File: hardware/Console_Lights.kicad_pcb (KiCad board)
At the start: 2 copper layers, 0 parts

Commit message: creat lib, add footprints, schematic updates
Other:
- board outline added: 60 x 20 mm
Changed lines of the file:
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@@
     (area 0 0 0 0)
     (thickness 1.6)
-    (drawings 0)
+    (drawings 4)
     (tracks 0)
     (zones 0)
@@
     (uvia_drill 0.1)
   )
+  (gr_line (start 110 110) (end 110 90) (layer Edge.Cuts) (width 0.15))
+  (gr_line (start 170 110) (end 110 110) (layer Edge.Cuts) (width 0.15))
+  (gr_line (start 170 90) (end 170 110) (layer Edge.Cuts) (width 0.15))
+  (gr_line (start 110 90) (end 170 90) (layer Edge.Cuts) (width 0.15))
 )

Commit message: add footprints, BOM, schematic updates
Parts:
- added REF**: POST, ConsoleLights:POST, F.Cu at (158.1, 113.0)
- added REF**: POST, ConsoleLights:POST, F.Cu at (120.0, 113.0)
- added REF**: POST, ConsoleLights:POST, F.Cu at (158.1, 94.0)
- added REF**: POST, ConsoleLights:POST, F.Cu at (120.0, 94.0)
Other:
- board size 60 x 20 mm -> 60 x 30 mm
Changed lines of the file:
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@@
     (links 0)
     (no_connects 0)
-    (area 0 0 0 0)
+    (area 109.924999 89.924999 170.075001 110.075001)
     (thickness 1.6)
     (drawings 4)
     (tracks 0)
     (zones 0)
-    (modules 0)
+    (modules 4)
     (nets 1)
   )
@@
     (uvia_drill 0.1)
   )
-  (gr_line (start 110 110) (end 110 90) (layer Edge.Cuts) (width 0.15))
-  (gr_line (start 170 110) (end 110 110) (layer Edge.Cuts) (width 0.15))
-  (gr_line (start 170 90) (end 170 110) (layer Edge.Cuts) (width 0.15))
+  (module ConsoleLights:POST (layer F.Cu)
+    (at 158.1 113.05)
+    (fp_text reference REF** (at 0 3) (layer F.SilkS)
+      (effects (font (size 1 1) (thickness 0.15)))
+    )
+    (fp_text value POST (at 0 -3) (layer F.Fab)
+      (effects (font (size 1 1) (thickness 0.15)))
+    )
+    (pad 0 thru_hole circle (at 0 0) (size 4.2 4.2) (drill 2.2) (layers *.Cu *.Mask))
+  )
+  (module ConsoleLights:POST (layer F.Cu)
+    (at 120 113.05)
+    (fp_text reference REF** (at 0 3) (layer F.SilkS)
+      (effects (font (size 1 1) (thickness 0.15)))
+    )
+    (fp_text value POST (at 0 -3) (layer F.Fab)
+      (effects (font (size 1 1) (thickness 0.15)))
+    )
+    (pad 0 thru_hole circle (at 0 0) (size 4.2 4.2) (drill 2.2) (layers *.Cu *.Mask))
+  )
+  (module ConsoleLights:POST (layer F.Cu)
+    (at 158.1 94)
+    (fp_text reference REF** (at 0 3) (layer F.SilkS)
+      (effects (font (size 1 1) (thickness 0.15)))
+    )
+    (fp_text value POST (at 0 -3) (layer F.Fab)
+      (effects (font (size 1 1) (thickness 0.15)))
+    )
+    (pad 0 thru_hole circle (at 0 0) (size 4.2 4.2) (drill 2.2) (layers *.Cu *.Mask))
+  )
+  (module ConsoleLights:POST (layer F.Cu)
+    (at 120 94)
+    (fp_text reference REF** (at 0 3) (layer F.SilkS)
+      (effects (font (size 1 1) (thickness 0.15)))
+    )
+    (fp_text value POST (at 0 -3) (layer F.Fab)
+      (effects (font (size 1 1) (thickness 0.15)))
+    )
+    (pad 0 thru_hole circle (at 0 0) (size 4.2 4.2) (drill 2.2) (layers *.Cu *.Mask))
+  )
+  (gr_line (start 110 120) (end 110 90) (layer Edge.Cuts) (width 0.15))
+  (gr_line (start 170 120) (end 110 120) (layer Edge.Cuts) (width 0.15))
+  (gr_line (start 170 90) (end 170 120) (layer Edge.Cuts) (width 0.15))
   (gr_line (start 110 90) (end 170 90) (layer Edge.Cuts) (width 0.15))
 )

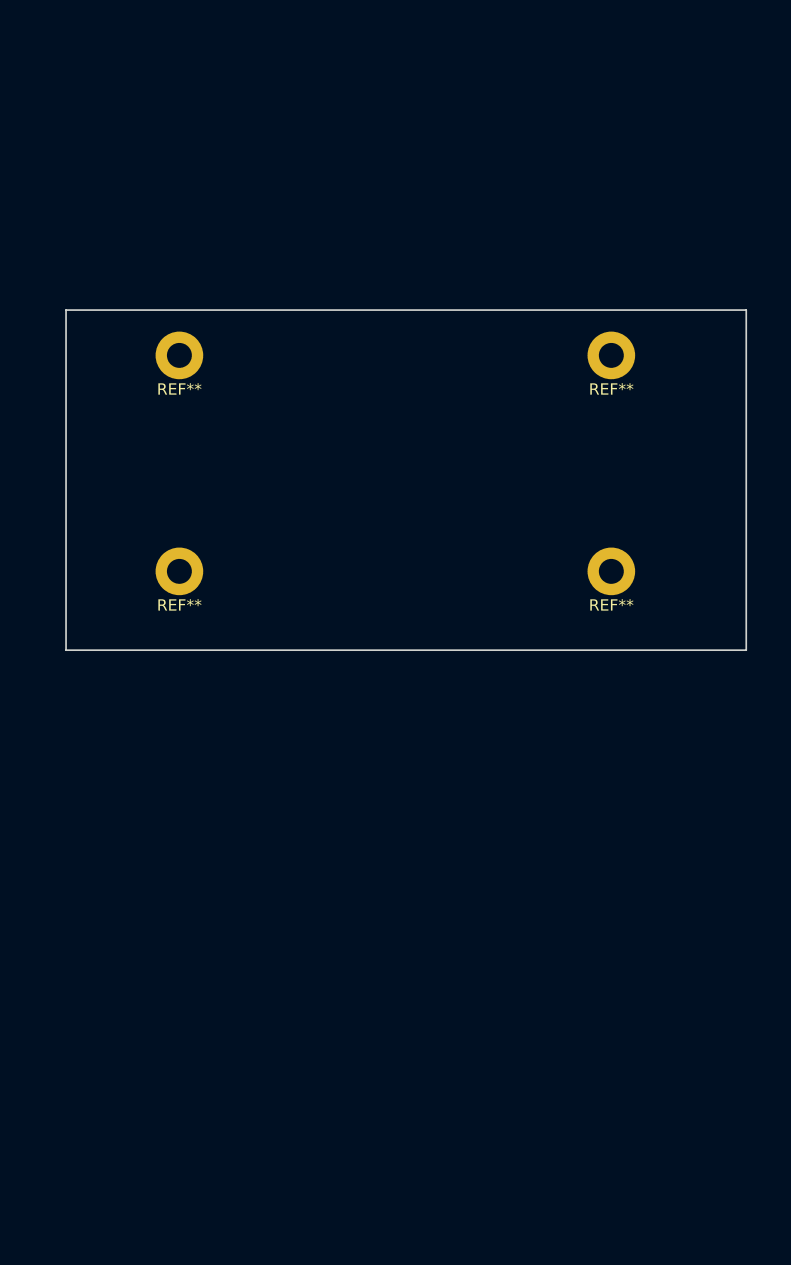
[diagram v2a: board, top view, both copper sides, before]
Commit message: BOM, footprint updates
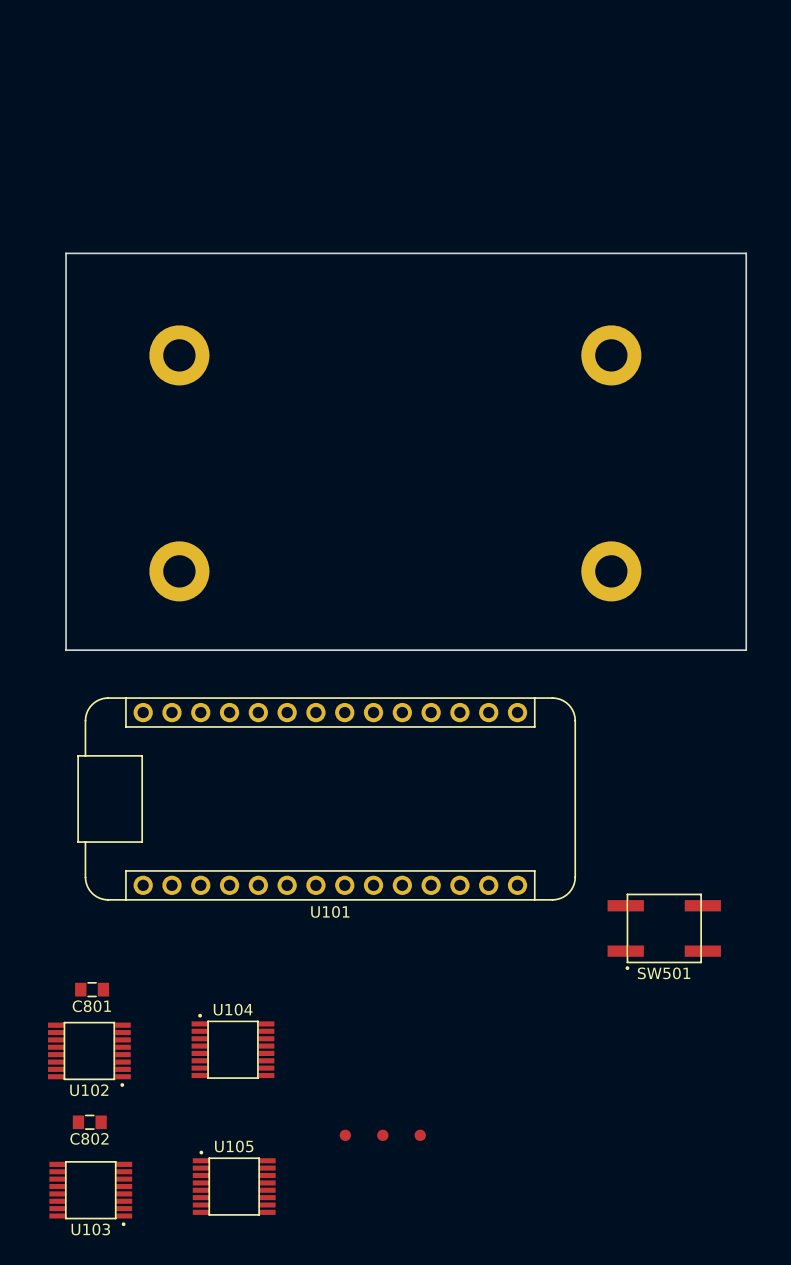
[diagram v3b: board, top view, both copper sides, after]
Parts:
- added C801: 1uF, ConsoleLights:C_0603, F.Cu at (112.3, 149.9)
- added C802: 1uF, ConsoleLights:C_0603, F.Cu at (112.1, 161.6)
- added SW501: SWITCH, ConsoleLights:Panasonic_Tac_Switch_EVQ-Q2K03W, F.Cu at (162.8, 144.5)
- added U101: Metro_Mini, ConsoleLights:Metro_Mini, F.Cu at (133.3, 133.1)
- added U102: 74HC595_SHIFT_REGISTER, ConsoleLights:16-TSSOP, F.Cu at (112.1, 155.4)
- added U103: 74HC595_SHIFT_REGISTER, ConsoleLights:16-TSSOP, F.Cu at (112.2, 167.6)
- added U104: ULN2003A_DARLINGTON_ARRAY, ConsoleLights:16-TSSOP, F.Cu at (124.7, 155.2)
- added U105: ULN2003A_DARLINGTON_ARRAY, ConsoleLights:16-TSSOP, F.Cu at (124.8, 167.3)
- added fid1: FID, ConsoleLights:Fiducial, F.Cu at (134.6, 162.8)
- added fid2: FID, ConsoleLights:Fiducial, F.Cu at (137.9, 162.8)
- added fid3: FID, ConsoleLights:Fiducial, F.Cu at (141.2, 162.8)
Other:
- board size 60 x 30 mm -> 60 x 35 mm

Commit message: add regulator, BOM, schematic, layout updates
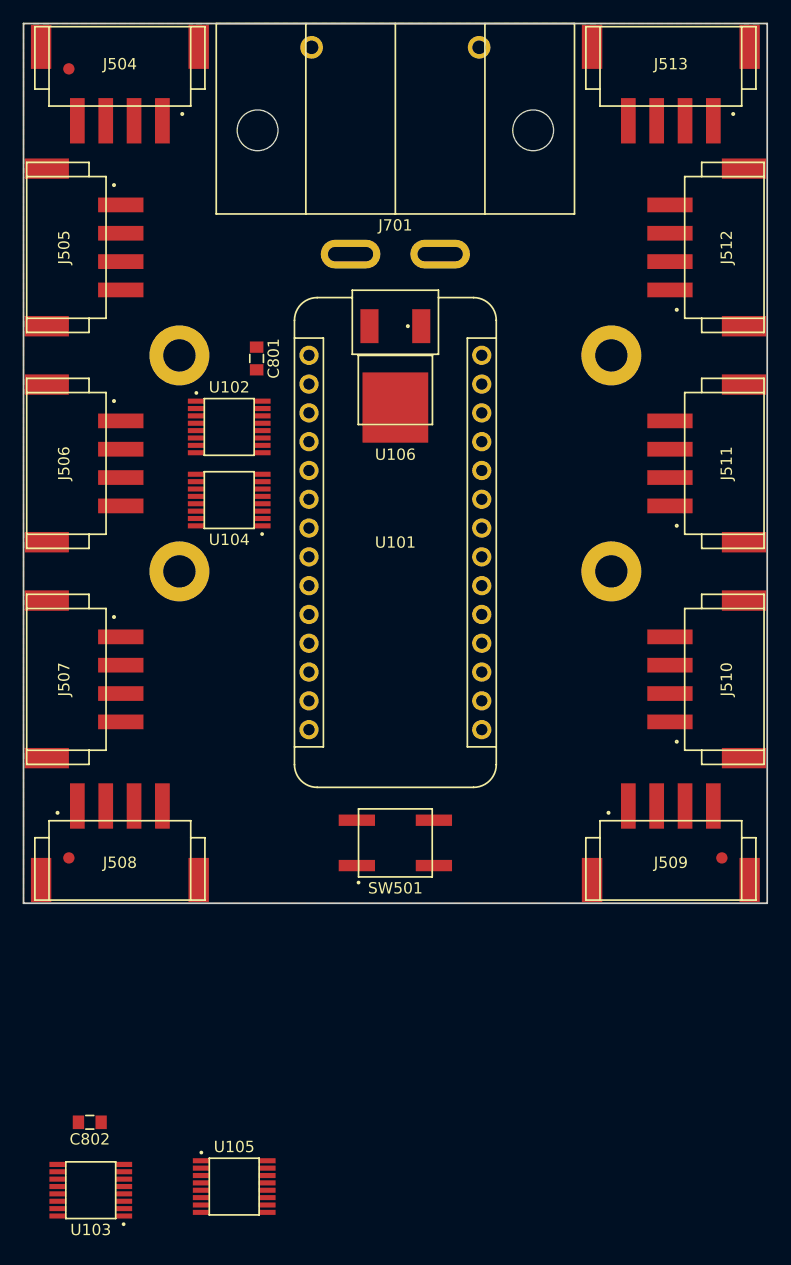
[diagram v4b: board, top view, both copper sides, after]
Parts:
- added J504: JST_Conn, ConsoleLights:S4B-XH-SM4-TB, F.Cu at (114.8, 64.7)
- added J505: JST_Conn, ConsoleLights:S4B-XH-SM4-TB, F.Cu at (106.2, 84.5)
- added J506: JST_Conn, ConsoleLights:S4B-XH-SM4-TB, F.Cu at (106.2, 103.5)
- added J507: JST_Conn, ConsoleLights:S4B-XH-SM4-TB, F.Cu at (106.2, 122.6)
- added J508: JST_Conn, ConsoleLights:S4B-XH-SM4-TB, F.Cu at (114.8, 142.3)
- added J509: JST_Conn, ConsoleLights:S4B-XH-SM4-TB, F.Cu at (163.3, 142.3)
- added J510: JST_Conn, ConsoleLights:S4B-XH-SM4-TB, F.Cu at (171.9, 122.6)
- added J511: JST_Conn, ConsoleLights:S4B-XH-SM4-TB, F.Cu at (171.9, 103.5)
- added J512: JST_Conn, ConsoleLights:S4B-XH-SM4-TB, F.Cu at (171.9, 84.5)
- added J513: JST_Conn, ConsoleLights:S4B-XH-SM4-TB, F.Cu at (163.3, 64.7)
- added J701: Conn_01x02, ConsoleLights:ASMPR45-1X2-RK_Wings, F.Cu at (139.1, 81.5)
- added U106: NCP1117-5_DPAK, ConsoleLights:DPAK_TO-252, F.Cu at (139.1, 95.5)
- moved fid1 97.2 mm to (110.2, 68.7)
- moved C801 57.5 mm to (126.8, 94.3), turned to 90 degrees
- moved U102 56.4 mm to (124.4, 100.3), turned to 0 degrees
- moved U104 48.5 mm to (124.4, 106.8), turned to 180 degrees
- moved fid2 37.0 mm to (110.2, 138.3)
- moved fid3 36.1 mm to (167.8, 138.3)
- moved SW501 24.9 mm to (139.1, 137.0)
- moved U101 23.3 mm to (139.1, 110.5), turned to 270 degrees
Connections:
- net Net-(U101-Pad10) renamed /SWITCH_8
- net Net-(U101-Pad12) renamed /SWITCH_9
- net Net-(U101-Pad7) renamed /SWITCH_5
- net Net-(U101-Pad8) renamed /SWITCH_6
- net Net-(U101-Pad9) renamed /SWITCH_7
- net Net-(U104-Pad10) renamed /LED_6
- net Net-(U104-Pad11) renamed /LED_5
- net Net-(U105-Pad14) renamed /LED_9
- net Net-(U105-Pad15) renamed /LED_8
- net Net-(U105-Pad16) renamed /LED_7
- SW501 pad 1: Net-(SW501-Pad1) -> GND
- SW501 pad 2: Net-(SW501-Pad2) -> /MODE
- U101 pad 19: Net-(U101-Pad19) -> /MODE
- U101 pad 2: Net-(U101-Pad2) -> /SWITCH_0
- U101 pad 26: Net-(U101-Pad26) -> +5V
- U101 pad 3: Net-(U101-Pad3) -> /SWITCH_1
- U101 pad 4: Net-(U101-Pad4) -> /SWITCH_2
- U101 pad 5: Net-(U101-Pad5) -> /SWITCH_3
- U101 pad 6: Net-(U101-Pad6) -> /SWITCH_4
- U104 pad 12: Net-(U104-Pad12) -> /LED_4
- U104 pad 13: Net-(U104-Pad13) -> /LED_3
- U104 pad 14: Net-(U104-Pad14) -> /LED_2
- U104 pad 15: Net-(U104-Pad15) -> /LED_1
- U104 pad 16: Net-(U104-Pad16) -> /LED_0
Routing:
- added copper zone on F.Cu, net GND
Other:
- board size 60 x 35 mm -> 65.6 x 77.6 mm

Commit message: mounting plate outline, floor-planning
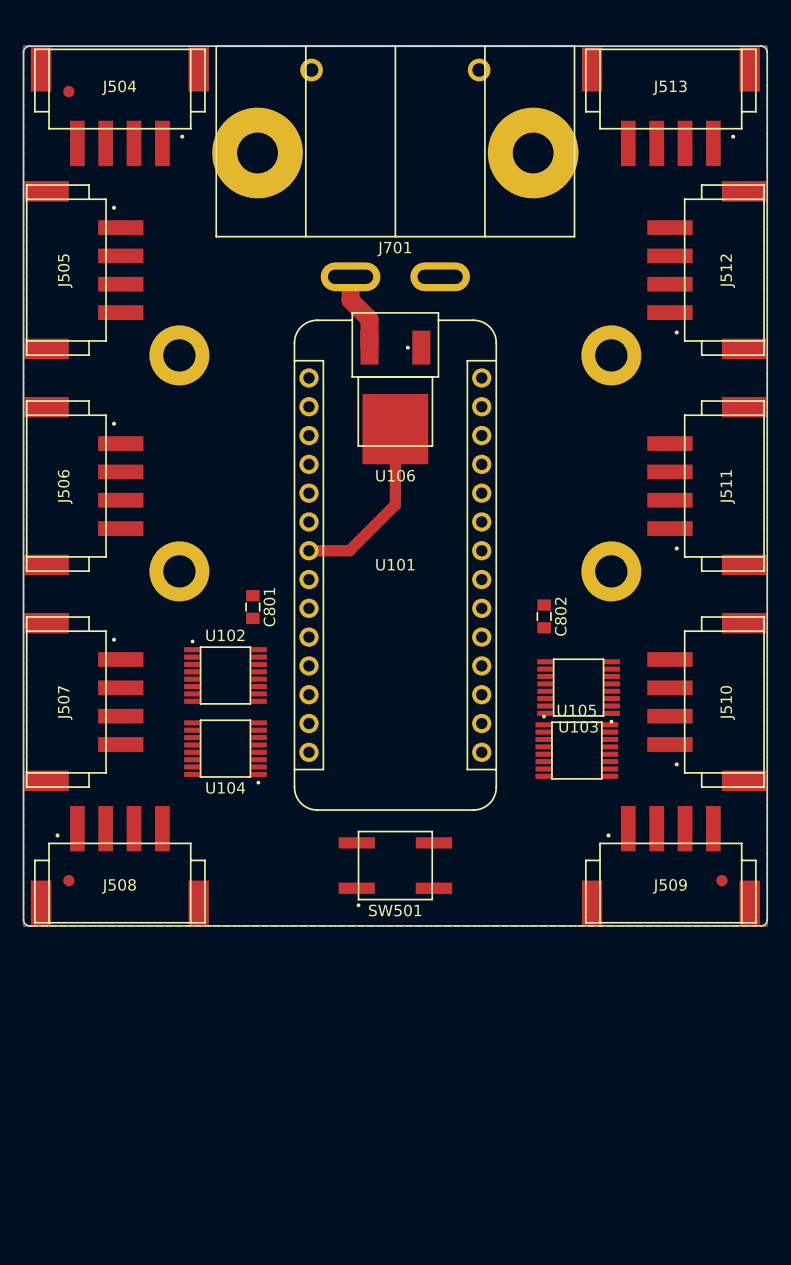
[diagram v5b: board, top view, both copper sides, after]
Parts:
- moved U103 61.8 mm to (155.2, 123.3)
- moved C802 60.0 mm to (152.2, 117.0), turned to 90 degrees
- moved U105 48.9 mm to (155.1, 128.9)
- moved C801 21.9 mm to (126.5, 116.2)
- moved U102 21.9 mm to (124.1, 122.2)
- moved U104 21.9 mm to (124.1, 128.7)
- moved J504 2.00 mm to (114.8, 66.7)
- moved J505 2.00 mm to (106.2, 86.5)
- moved J506 2.00 mm to (106.2, 105.5)
- moved J507 2.00 mm to (106.2, 124.6)
- moved J508 2.00 mm to (114.8, 144.3)
- moved J509 2.00 mm to (163.3, 144.3)
- moved J510 2.00 mm to (171.9, 124.6)
- moved J511 2.00 mm to (171.9, 105.5)
- moved J512 2.00 mm to (171.9, 86.5)
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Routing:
- net +5V: track 0.00 -> 16.0 mm
- net +12V: track 0.00 -> 6.94 mm
- added copper zone on B.Cu, net GND
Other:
- outline, holes or cut-outs redrawn

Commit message: schematic/routing update
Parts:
- added REF**: GND_Stitch_Via, ConsoleLights:GND_Stitch_Via, F.Cu at (149.4, 108.5)
- added REF**: GND_Stitch_Via, ConsoleLights:GND_Stitch_Via, F.Cu at (114.8, 92.2)
- added REF**: GND_Stitch_Via, ConsoleLights:GND_Stitch_Via, F.Cu at (109.2, 75.3)
- added REF**: GND_Stitch_Via, ConsoleLights:GND_Stitch_Via, F.Cu at (157.7, 75.3)
- added REF**: GND_Stitch_Via, ConsoleLights:GND_Stitch_Via, F.Cu at (163.3, 81.0)
- added REF**: GND_Stitch_Via, ConsoleLights:GND_Stitch_Via, F.Cu at (163.3, 99.9)
- added REF**: GND_Stitch_Via, ConsoleLights:GND_Stitch_Via, F.Cu at (168.8, 135.7)
- added REF**: GND_Stitch_Via, ConsoleLights:GND_Stitch_Via, F.Cu at (128.7, 104.0)
- added REF**: GND_Stitch_Via, ConsoleLights:GND_Stitch_Via, F.Cu at (163.3, 118.8)
- added REF**: GND_Stitch_Via, ConsoleLights:GND_Stitch_Via, F.Cu at (152.9, 100.5)
- added REF**: GND_Stitch_Via, ConsoleLights:GND_Stitch_Via, F.Cu at (125.2, 99.8)
- added REF**: GND_Stitch_Via, ConsoleLights:GND_Stitch_Via, F.Cu at (158.8, 98.5)
- added REF**: GND_Stitch_Via, ConsoleLights:GND_Stitch_Via, F.Cu at (119.3, 103.1)
- added REF**: GND_Stitch_Via, ConsoleLights:GND_Stitch_Via, F.Cu at (120.4, 135.7)
- added REF**: GND_Stitch_Via, ConsoleLights:GND_Stitch_Via, F.Cu at (114.8, 130.3)
- added REF**: GND_Stitch_Via, ConsoleLights:GND_Stitch_Via, F.Cu at (114.8, 111.2)
- moved U105 22.6 mm to (154.1, 106.2)
- moved U103 22.5 mm to (154.1, 100.8)
- moved U104 22.4 mm to (124.0, 106.2)
- moved C802 22.0 mm to (151.2, 95.0)
- moved U102 21.4 mm to (124.0, 100.8)
- moved C801 21.2 mm to (126.9, 95.0)
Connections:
- J509 pad 2: /SWITCH_0 -> /SWITCH_5
- J509 pad 3: /LED_0 -> /LED_5
- J510 pad 2: /SWITCH_0 -> /SWITCH_6
- J510 pad 3: /LED_0 -> /LED_6
- J511 pad 2: /SWITCH_0 -> /SWITCH_7
- J511 pad 3: /LED_0 -> /LED_7
- J512 pad 2: /SWITCH_0 -> /SWITCH_8
- J512 pad 3: /LED_0 -> /LED_8
- J513 pad 2: /SWITCH_0 -> /SWITCH_9
- J513 pad 3: /LED_0 -> /LED_9
- U101 pad 10: /SWITCH_8 -> /SWITCH_0
- U101 pad 11: Net-(U101-Pad11) -> /DATA
- U101 pad 13: Net-(U101-Pad13) -> /CLOCK
- U101 pad 2: /SWITCH_0 -> /SWITCH_4
- U101 pad 3: /SWITCH_1 -> /SWITCH_5
- U101 pad 4: /SWITCH_2 -> /SWITCH_3
- U101 pad 5: /SWITCH_3 -> /SWITCH_6
- U101 pad 6: /SWITCH_4 -> /SWITCH_2
- U101 pad 7: /SWITCH_5 -> /SWITCH_7
- U101 pad 8: /SWITCH_6 -> /SWITCH_1
- U101 pad 9: /SWITCH_7 -> /SWITCH_8
- U102 pad 14: /DATA -> Net-(U102-Pad14)
- U103 pad 14: Net-(U102-Pad9) -> /DATA
- U103 pad 9: Net-(U103-Pad9) -> Net-(U102-Pad14)
- U104 pad 10: /LED_6 -> Net-(U104-Pad10)
- U104 pad 11: /LED_5 -> Net-(U104-Pad11)
- U104 pad 12: /LED_4 -> /LED_0
- U104 pad 13: /LED_3 -> /LED_1
- U104 pad 15: /LED_1 -> /LED_3
- U104 pad 16: /LED_0 -> /LED_4
- U105 pad 12: Net-(U105-Pad12) -> /LED_5
- U105 pad 13: Net-(U105-Pad13) -> /LED_6
- U105 pad 14: /LED_9 -> /LED_7
- U105 pad 16: /LED_7 -> /LED_9
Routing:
- net +12V: track 6.94 -> 179.2 mm
- net /SWITCH_0: track 0.00 -> 50.0 mm, vias 0 -> 1
- net /SWITCH_4: track 0.00 -> 42.7 mm, vias 0 -> 1
- net /SWITCH_3: track 0.00 -> 40.5 mm, vias 0 -> 1
- net /SWITCH_9: track 0.00 -> 37.2 mm, vias 0 -> 1
- net /SWITCH_5: track 0.00 -> 27.3 mm, vias 0 -> 1
- net /LED_6: track 0.00 -> 25.1 mm
- net /SWITCH_6: track 0.00 -> 20.5 mm
- net /MODE: track 0.00 -> 16.5 mm
- net GND: track 0.00 -> 11.0 mm
- net Net-(U102-Pad5): track 0.00 -> 10.3 mm
- net Net-(U102-Pad7): track 0.00 -> 9.68 mm
- net Net-(U102-Pad4): track 0.00 -> 9.67 mm
- net Net-(U102-Pad2): track 0.00 -> 9.67 mm
- net Net-(U102-Pad3): track 0.00 -> 9.67 mm
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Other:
- board text added: "MODE"

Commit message: routing updates
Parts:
- moved fid1 1.41 mm to (111.2, 69.7)
- moved fid2 1.41 mm to (111.2, 141.3)
- moved fid3 1.41 mm to (166.8, 141.3)
- moved REF** 0.65 mm to (149.4, 107.9)
- moved REF** 0.65 mm to (128.7, 104.6)
- moved REF** 0.65 mm to (119.3, 102.4)
- moved REF** 0.65 mm to (158.8, 99.2)
- moved REF** 0.33 mm to (163.3, 80.7)
- moved REF** 0.26 mm to (169.1, 135.7)
- moved REF** 0.16 mm to (109.0, 75.3)
- moved REF** 0.16 mm to (163.3, 99.8)
- moved REF** 0.08 mm to (120.5, 135.7)
- moved REF** 0.06 mm to (163.3, 118.8)
- moved REF** 0.06 mm to (157.6, 75.3)
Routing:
- net /SWITCH_2: track 0.00 -> 62.3 mm, vias 0 -> 1
- net /LED_0: track 0.00 -> 43.3 mm, vias 0 -> 2
- net +12V: track 179.2 -> 222.4 mm
- net /SWITCH_1: track 0.00 -> 41.6 mm, vias 0 -> 1
- net /LED_5: track 0.00 -> 39.4 mm, vias 0 -> 2
- net Net-(U102-Pad14): track 0.00 -> 34.6 mm
- net /LED_9: track 0.00 -> 34.6 mm, vias 0 -> 2
- net /LED_4: track 0.00 -> 32.3 mm
- net /LED_1: track 0.00 -> 31.0 mm, vias 0 -> 2
- net +5V: track 18.5 -> 49.3 mm, vias 0 -> 4
- net /LED_8: track 0.00 -> 28.2 mm, vias 0 -> 2
- net /SWITCH_8: track 0.00 -> 27.7 mm, vias 0 -> 1
- net /CLOCK: track 6.89 -> 33.1 mm
- net /LED_3: track 0.00 -> 25.1 mm, vias 0 -> 2
- net /SWITCH_7: track 0.00 -> 18.4 mm, vias 0 -> 1
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
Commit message: routing updates, logo
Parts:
- added REF**: GND_Stitch_Via, ConsoleLights:GND_Stitch_Via, F.Cu at (139.1, 141.0)
- added REF**: GND_Stitch_Via, ConsoleLights:GND_Stitch_Via, F.Cu at (149.4, 106.6)
- added REF**: GND_Stitch_Via, ConsoleLights:GND_Stitch_Via, F.Cu at (128.7, 105.9)
- moved U106 0.40 mm to (139.1, 97.0)
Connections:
- U101 pad 10: /SWITCH_0 -> +5V
- U101 pad 12: /SWITCH_9 -> /LATCH
- U101 pad 14: Net-(U101-Pad14) -> /SWITCH_1
- U101 pad 15: Net-(U101-Pad15) -> /SWITCH_0
- U101 pad 16: Net-(U101-Pad16) -> /SWITCH_9
- U101 pad 8: /SWITCH_1 -> Net-(U101-Pad8)
- U102 pad 11: /LATCH -> /CLOCK
- U102 pad 12: /CLOCK -> /LATCH
- U103 pad 11: /LATCH -> /CLOCK
- U103 pad 12: /CLOCK -> /LATCH
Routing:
- net /SWITCH_9: track 31.7 -> 62.2 mm
- net +5V: track 49.3 -> 61.8 mm
- net /SWITCH_0: track 48.1 -> 58.3 mm
- net /LATCH: track 0.00 -> 5.34 mm
- net /SWITCH_1: track 41.6 -> 44.1 mm
- net +12V: track 222.4 -> 221.1 mm
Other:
- board text added: "+"
- board text added: "-"
